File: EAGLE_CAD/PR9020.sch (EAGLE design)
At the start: 72 parts, among them SW1 C&K_PTS645, U1 SI4702-C19-GMR, X1 ABS25XTAL

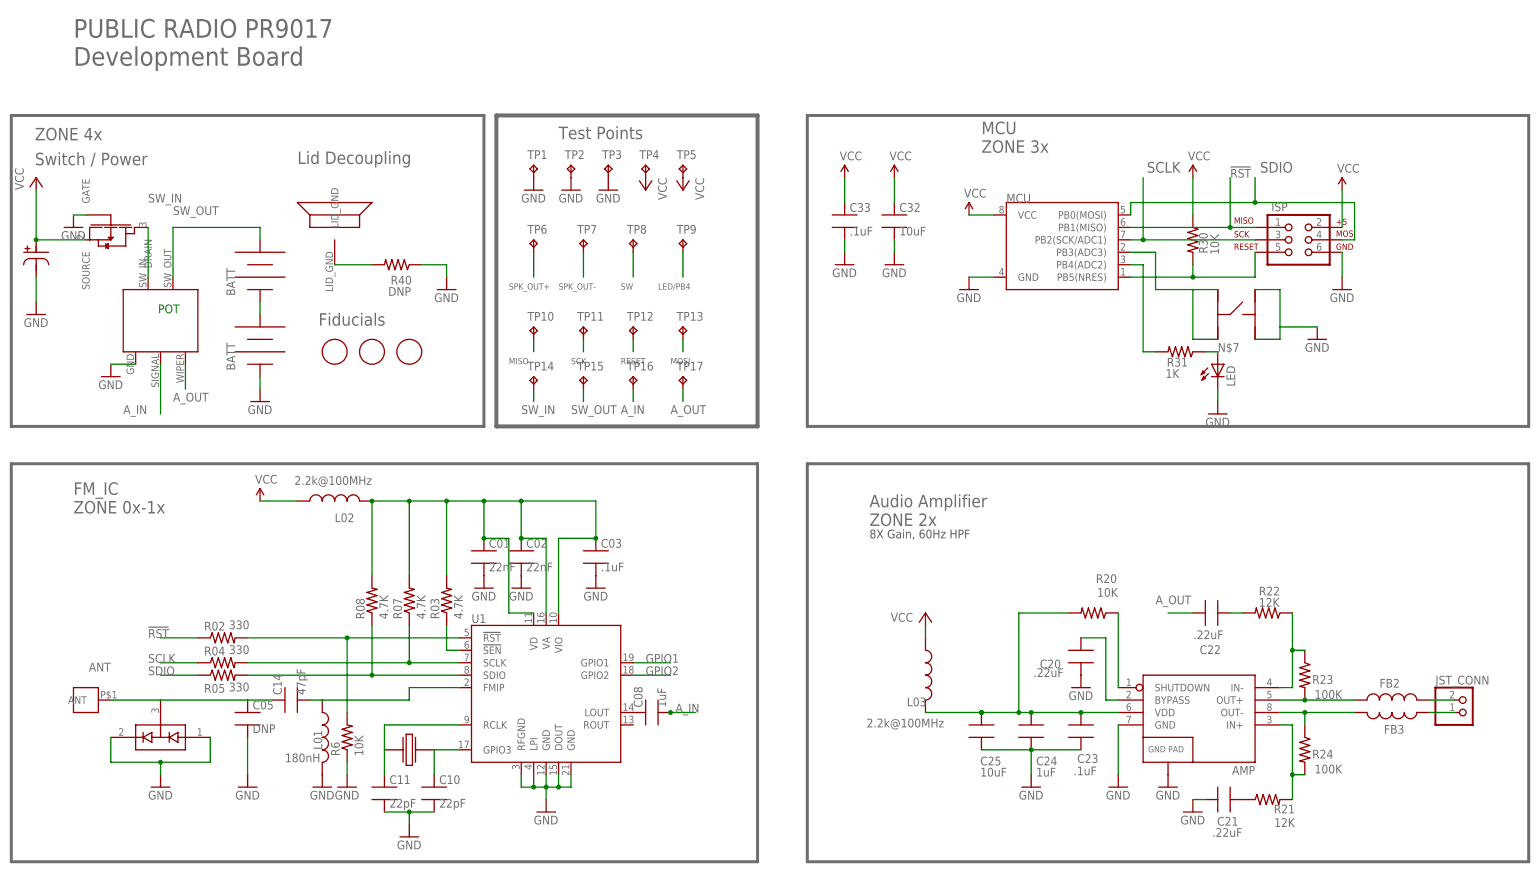
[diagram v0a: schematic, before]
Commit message: Bumped to 9020
Changed Led package to 0805 to conform to PR9019 BOM
Exported Gerbers
Updated SCH and board text to read ‘9020’
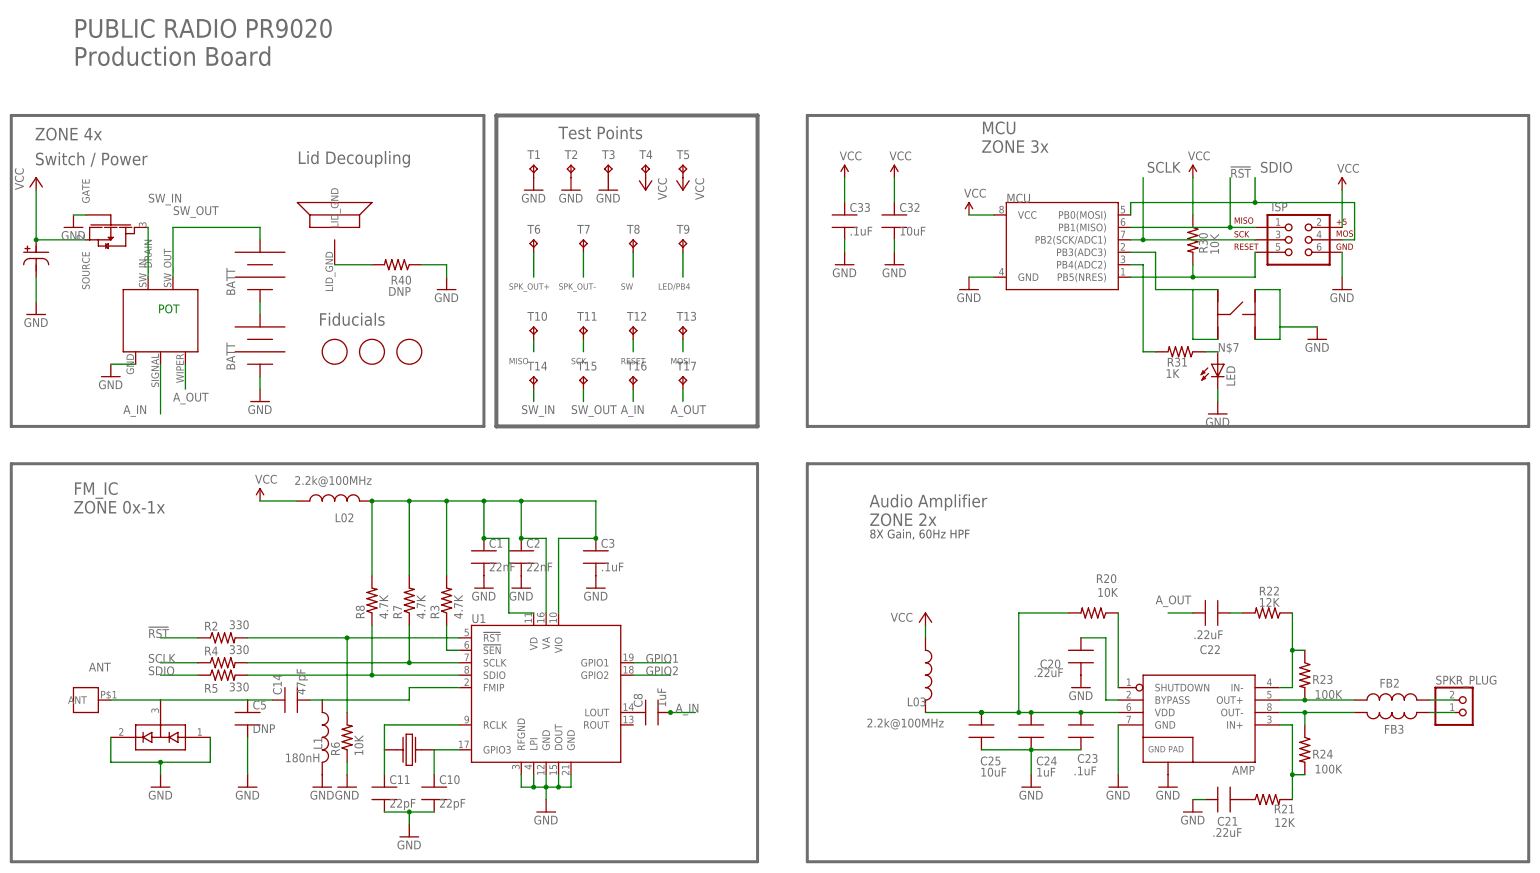
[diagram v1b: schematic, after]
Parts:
- JP5, JP6: MFG_PN (none) -> 2 of BK92 - supplied by CL Labs
- LED: value LED -> (none); device PR_Parts_Library:LED -> adafruit:LEDCHIPLED_0805
- R1: MFG_PN (none) -> RV170SF-43-20F-A10K - supplied by CL Labs
- R21, R22: MFG_PN RMCF0603FT12K0 -> RC0603FR-0712KL
- R23, R24: MFG_PN RMCF0603FT100K -> ERJ-3EKF1003V
- U1: MFG_PN (none) -> Si4702 C19 GM - supplied by CL Labs
- renumbered C01 to C1, C02 to C2, C03 to C3, C05 to C5, C08 to C8, JST_CONN to SPKR_PLUG, L01 to L1, R02 to R2, R03 to R3, R04 to R4, R05 to R5, R07 to R7, R08 to R8, TP1 to T1, TP10 to T10, TP11 to T11, TP12 to T12, TP13 to T13, TP14 to T14, TP15 to T15, TP16 to T16, TP17 to T17, TP2 to T2, TP3 to T3, TP4 to T4, TP5 to T5, TP6 to T6, TP7 to T7, TP8 to T8, TP9 to T9
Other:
- note added: "PUBLIC RADIO PR9020 Production Board"
- note removed: "PUBLIC RADIO PR9017 Development Board"

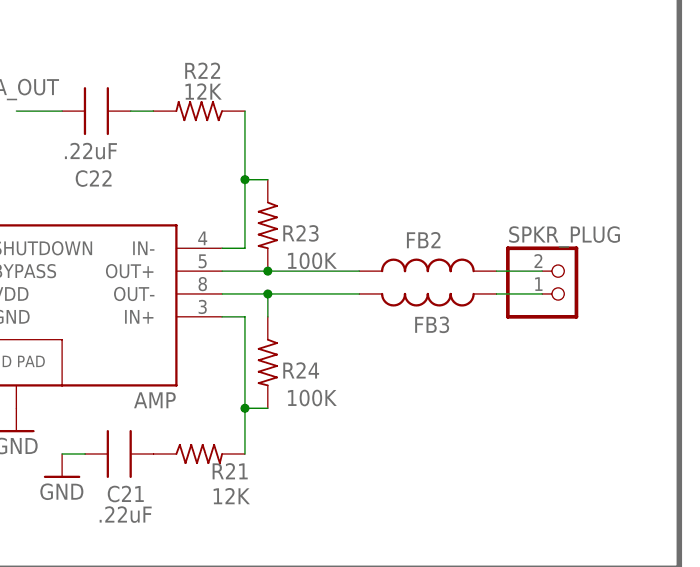
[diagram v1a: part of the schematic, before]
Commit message: Updated MFG#s
Changed ferrite beads to 0 ohm resistors
Removed ‘dnp’ from R40
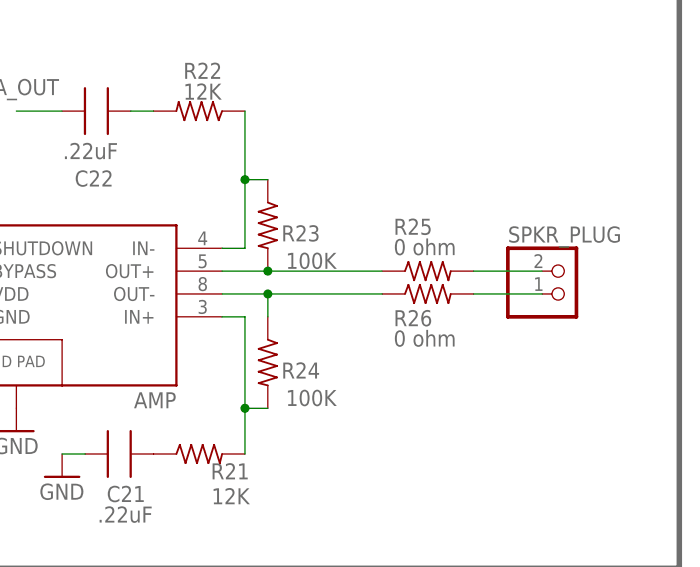
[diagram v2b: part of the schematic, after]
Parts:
- removed FB2, FB3: (no value), PR_Parts_Library:L_SMT_0805_ADAFRUIT
- added R25, R26: 0 ohm, PR_Parts_Library:R_SMT_0805_ADAFRUIT
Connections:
- net N$11: now also R26.1; no longer FB3.2
- net N$4: now also R25.1; no longer FB2.1
- net SPK_OUT+: now also R25.2; no longer FB2.2
- net SPK_OUT-: now also R26.2; no longer FB3.1
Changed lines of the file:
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@@
 <?xml version="1.0" encoding="utf-8"?>
 <!DOCTYPE eagle SYSTEM "eagle.dtd">
-<eagle version="6.6.0">
+<eagle version="7.2.0">
 <drawing>
 <settings>
@@
 </part>
 <part name="GND10" library="SparkFun-Aesthetics" deviceset="GND" device=""/>
-<part name="FB2" library="PR_Parts_Library" deviceset="L_SMT" device="_0805_ADAFRUIT">
-<attribute name="CURRENT" value="2A"/>
-<attribute name="DCR" value="45m"/>
-<attribute name="MFG_PN" value="HI0805R800R-10"/>
-</part>
-<part name="FB3" library="PR_Parts_Library" deviceset="L_SMT" device="_0805_ADAFRUIT">
-<attribute name="CURRENT" value="2A"/>
-<attribute name="DCR" value="45m"/>
-<attribute name="MFG_PN" value="HI0805R800R-10"/>
-</part>
 <part name="R30" library="PR_Parts_Library" deviceset="R_SMT" device="_R0603_CPL" value="10K">
 <attribute name="MFG_PN" value="ERJ-3GEYJ103V"/>
@@
 <part name="LED" library="adafruit" deviceset="LED" device="CHIPLED_0805">
 <attribute name="MFG_PN" value="LY R976-PS-36"/>
+</part>
+<part name="R25" library="PR_Parts_Library" deviceset="R_SMT" device="_0805_ADAFRUIT" value="0 ohm">
+<attribute name="MFG_PN" value="ERJ-6GEY0R00V
+"/>
+</part>
+<part name="R26" library="PR_Parts_Library" deviceset="R_SMT" device="_0805_ADAFRUIT" value="0 ohm">
+<attribute name="MFG_PN" value="ERJ-6GEY0R00V
+"/>
 </part>
 </parts>
@@
 <instance part="JP6" gate="BATT" x="10.16" y="106.68" rot="R90"/>
 <instance part="GND10" gate="1" x="10.16" y="93.98"/>
-<instance part="FB2" gate="G$1" x="241.3" y="33.02" smashed="yes" rot="R90">
-<attribute name="NAME" x="238.76" y="35.56" size="1.778" layer="95"/>
-<attribute name="VALUE" x="246.38" y="35.56" size="1.778" layer="96" rot="R90"/>
-</instance>
-<instance part="FB3" gate="G$1" x="241.3" y="30.48" smashed="yes" rot="R270">
-<attribute name="NAME" x="243.84" y="27.94" size="1.778" layer="95" rot="R180"/>
-<attribute name="VALUE" x="236.22" y="27.94" size="1.778" layer="96" rot="R270"/>
-</instance>
 <instance part="R30" gate="G$1" x="200.66" y="127" smashed="yes" rot="R270">
 <attribute name="NAME" x="203.6826" y="124.206" size="1.778" layer="95" rot="R90"/>
@@
 <instance part="LED" gate="G$1" x="205.74" y="101.6">
 <attribute name="MFG_PN" x="205.74" y="101.6" size="1.778" layer="96" display="off"/>
+</instance>
+<instance part="R25" gate="G$1" x="241.3" y="33.02" smashed="yes">
+<attribute name="NAME" x="237.49" y="37.0586" size="1.778" layer="95"/>
+<attribute name="VALUE" x="237.49" y="34.798" size="1.778" layer="96"/>
+</instance>
+<instance part="R26" gate="G$1" x="241.3" y="30.48" smashed="yes">
+<attribute name="NAME" x="237.49" y="26.8986" size="1.778" layer="95"/>
+<attribute name="VALUE" x="237.49" y="24.638" size="1.778" layer="96"/>
 </instance>
 </instances>
@@
 </segment>
 <segment>
-<pinref part="FB2" gate="G$1" pin="2"/>
 <pinref part="SPKR_PLUG" gate="G$1" pin="1"/>
-<wire x1="248.92" y1="33.02" x2="254" y2="33.02" width="0.1524" layer="91"/>
+<wire x1="246.38" y1="33.02" x2="254" y2="33.02" width="0.1524" layer="91"/>
+<pinref part="R25" gate="G$1" pin="2"/>
 </segment>
 </net>
@@
 </segment>
 <segment>
-<pinref part="FB3" gate="G$1" pin="1"/>
 <pinref part="SPKR_PLUG" gate="G$1" pin="2"/>
-<wire x1="248.92" y1="30.48" x2="254" y2="30.48" width="0.1524" layer="91"/>
+<wire x1="246.38" y1="30.48" x2="254" y2="30.48" width="0.1524" layer="91"/>
+<pinref part="R26" gate="G$1" pin="2"/>
 </segment>
 </net>
@@
 <segment>
 <pinref part="AMP" gate="G$1" pin="OUT+"/>
-<pinref part="FB2" gate="G$1" pin="1"/>
 <wire x1="218.44" y1="33.02" x2="223.52" y2="33.02" width="0.1524" layer="91"/>
 <pinref part="R23" gate="G$1" pin="2"/>
-<wire x1="223.52" y1="33.02" x2="233.68" y2="33.02" width="0.1524" layer="91"/>
+<wire x1="223.52" y1="33.02" x2="236.22" y2="33.02" width="0.1524" layer="91"/>
 <junction x="223.52" y="33.02"/>
+<pinref part="R25" gate="G$1" pin="1"/>
 </segment>
 </net>
@@
 <segment>
 <pinref part="AMP" gate="G$1" pin="OUT-"/>
-<pinref part="FB3" gate="G$1" pin="2"/>
 <wire x1="218.44" y1="30.48" x2="223.52" y2="30.48" width="0.1524" layer="91"/>
 <pinref part="R24" gate="G$1" pin="1"/>
-<wire x1="223.52" y1="30.48" x2="233.68" y2="30.48" width="0.1524" layer="91"/>
+<wire x1="223.52" y1="30.48" x2="236.22" y2="30.48" width="0.1524" layer="91"/>
 <wire x1="223.52" y1="27.94" x2="223.52" y2="30.48" width="0.1524" layer="91"/>
 <junction x="223.52" y="30.48"/>
-</segment>
-</net>
+<pinref part="R26" gate="G$1" pin="1"/>
+</segment>
+</net>
